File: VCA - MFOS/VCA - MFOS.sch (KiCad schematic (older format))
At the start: 81 parts, among them J1 CVA1, J10 LINA, J11 OUTA, J12 CVB1, J13 CVB2, J14 Sig_In_B, J15 ADJB, J16 LOGB, J17 CMNB, J18 LINB, J19 OUTB, J2 CVA2, J3 Sig_In_A, J4 ADJA, J5 12V_Conn, J6 -12V_Conn, J7 Gnd_Conn, J8 LOGA, J9 CMNA, Q1 2N3904, Q2 2N3906, Q3 2N3904, Q4 2N3906, SW1 LOG_SW_A, SW2 LOG_SW_B, U1 TL084, U2 LM13700

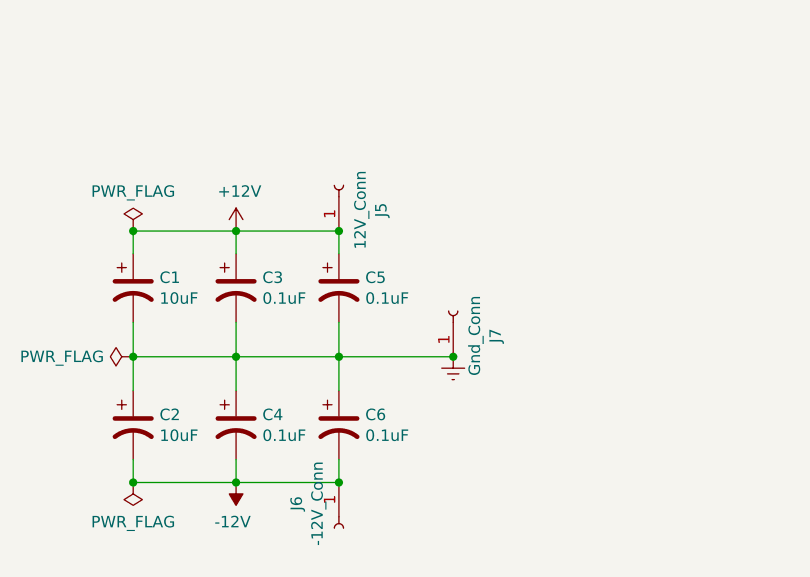
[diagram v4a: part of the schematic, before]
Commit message: pcb design for VCA finished
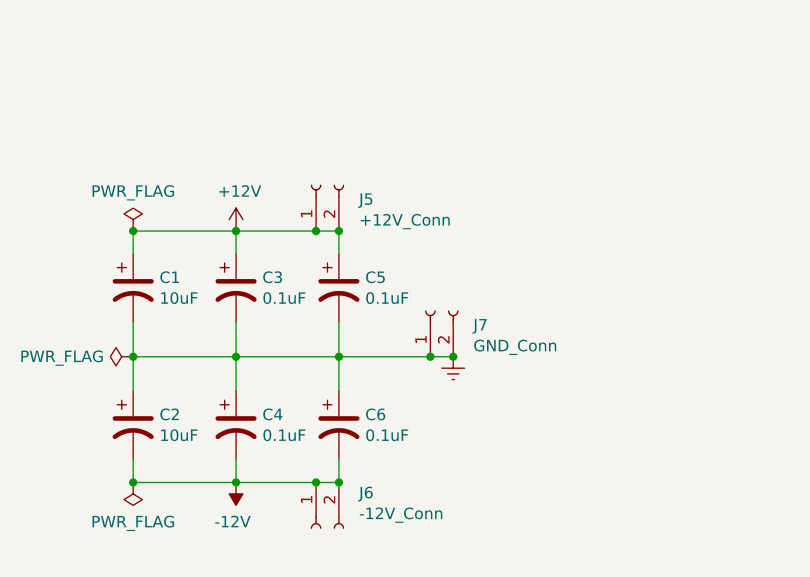
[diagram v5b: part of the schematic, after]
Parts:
- removed J5: 12V_Conn, Connector_Wire:SolderWirePad_1x02_P3.81mm_Drill1mm, symbol Connector:Conn_01x01_Female
- removed J6: -12V_Conn, Connector_Wire:SolderWirePad_1x02_P3.81mm_Drill1mm, symbol Connector:Conn_01x01_Female
- removed J7: Gnd_Conn, Connector_Wire:SolderWirePad_1x02_P3.81mm_Drill1mm, symbol Connector:Conn_01x01_Female
- added J5: +12V_Conn, Connector_Wire:SolderWirePad_1x02_P3.81mm_Drill1mm, symbol Connector:Conn_01x02_Female
- added J6: -12V_Conn, Connector_Wire:SolderWirePad_1x02_P3.81mm_Drill1mm, symbol Connector:Conn_01x02_Female
- added J7: GND_Conn, Connector_Wire:SolderWirePad_1x02_P3.81mm_Drill1mm, symbol Connector:Conn_01x02_Female
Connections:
- net +12V: now also J5.1 (Pin_1), J5.2 (Pin_2)
- net -12V: now also J6.1 (Pin_1), J6.2 (Pin_2)
- net Earth: now also J7.1 (Pin_1), J7.2 (Pin_2)
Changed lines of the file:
@@
 	2200 6400 2200 6300
 Wire Wire Line
-	2200 6300 1750 6300
+	2200 6300 2100 6300
 Wire Wire Line
 	1300 7300 1300 7400
@@
 Connection ~ 1750 7400
 Wire Wire Line
-	1750 7400 2200 7400
+	1750 7400 2100 7400
 Wire Wire Line
 	2200 7400 2200 7300
@@
 	2200 6700 2200 6850
 Wire Wire Line
-	2200 6850 2700 6850
+	2200 6850 2600 6850
 Connection ~ 2200 6850
 Wire Wire Line
@@
 NoConn ~ 2900 3850
 $Comp
-L Connector:Conn_01x01_Female J5
-U 1 1 6015D3CB
-P 2200 6100
-F 0 "J5" H 2092 6285 50  0000 C CNN
-F 1 "12V_Conn" H 2092 6194 50  0000 C CNN
-F 2 "Connector_Wire:SolderWirePad_1x02_P3.81mm_Drill1mm" H 2200 6100 50  0001 C CNN
-F 3 "~" H 2200 6100 50  0001 C CNN
-	1    2200 6100
-	0    1    -1   0
-$EndComp
-Connection ~ 2200 6300
-$Comp
-L Connector:Conn_01x01_Female J7
-U 1 1 6015E206
-P 2700 6650
-F 0 "J7" H 2592 6835 50  0000 C CNN
-F 1 "Gnd_Conn" H 2592 6744 50  0000 C CNN
-F 2 "Connector_Wire:SolderWirePad_1x02_P3.81mm_Drill1mm" H 2700 6650 50  0001 C CNN
-F 3 "~" H 2700 6650 50  0001 C CNN
-	1    2700 6650
-	0    1    -1   0
-$EndComp
-Connection ~ 2700 6850
-$Comp
-L Connector:Conn_01x01_Female J6
-U 1 1 6015EAA9
-P 2200 7600
-F 0 "J6" H 2092 7785 50  0000 C CNN
-F 1 "-12V_Conn" H 2092 7694 50  0000 C CNN
-F 2 "Connector_Wire:SolderWirePad_1x02_P3.81mm_Drill1mm" H 2200 7600 50  0001 C CNN
-F 3 "~" H 2200 7600 50  0001 C CNN
-	1    2200 7600
-	0    -1   1    0
-$EndComp
-Connection ~ 2200 7400
-$Comp
 L Amplifier_Operational:TL084 U1
 U 2 1 601B7B55
@@
 	-1   0    0    1
 $EndComp
+Connection ~ 2200 6300
+$Comp
+L Connector:Conn_01x02_Female J5
+U 1 1 5FF6A6A5
+P 2100 6100
+F 0 "J5" V 2038 5912 50  0000 R CNN
+F 1 "+12V_Conn" V 1947 5912 50  0000 R CNN
+F 2 "Connector_Wire:SolderWirePad_1x02_P3.81mm_Drill1mm" H 2100 6100 50  0001 C CNN
+F 3 "~" H 2100 6100 50  0001 C CNN
+	1    2100 6100
+	0    -1   -1   0
+$EndComp
+Wire Wire Line
+	1750 6300 2100 6300
+Connection ~ 2100 6300
+$Comp
+L Connector:Conn_01x02_Female J7
+U 1 1 5FF882B9
+P 2600 6650
+F 0 "J7" V 2538 6462 50  0000 R CNN
+F 1 "GND_Conn" V 2447 6462 50  0000 R CNN
+F 2 "Connector_Wire:SolderWirePad_1x02_P3.81mm_Drill1mm" H 2600 6650 50  0001 C CNN
+F 3 "~" H 2600 6650 50  0001 C CNN
+	1    2600 6650
+	0    -1   -1   0
+$EndComp
+Wire Wire Line
+	2600 6850 2700 6850
+Connection ~ 2600 6850
+Connection ~ 2700 6850
+$Comp
+L Connector:Conn_01x02_Female J6
+U 1 1 5FF9BBBD
+P 2100 7600
+F 0 "J6" V 1946 7412 50  0000 R CNN
+F 1 "-12V_Conn" V 2037 7412 50  0000 R CNN
+F 2 "Connector_Wire:SolderWirePad_1x02_P3.81mm_Drill1mm" H 2100 7600 50  0001 C CNN
+F 3 "~" H 2100 7600 50  0001 C CNN
+	1    2100 7600
+	0    -1   1    0
+$EndComp
+Wire Wire Line
+	2100 7400 2200 7400
+Connection ~ 2100 7400
+Connection ~ 2200 7400
 $EndSCHEMATC
